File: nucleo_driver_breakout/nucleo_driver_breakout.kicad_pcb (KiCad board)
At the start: 4 copper layers, 211 x 123 mm, 118 parts, among them J1 Conn_02x18_Odd_Even, J10 Conn_01x06_Pin, J11 Conn_01x06_Pin, J12 Conn_01x04_Pin, J13 Conn_01x04_Pin, J14 Conn_01x04_Pin, J15 Conn_01x04_Pin, J16 Conn_01x02_Pin, J17 Conn_01x02_Pin, J18 Conn_01x02_Pin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

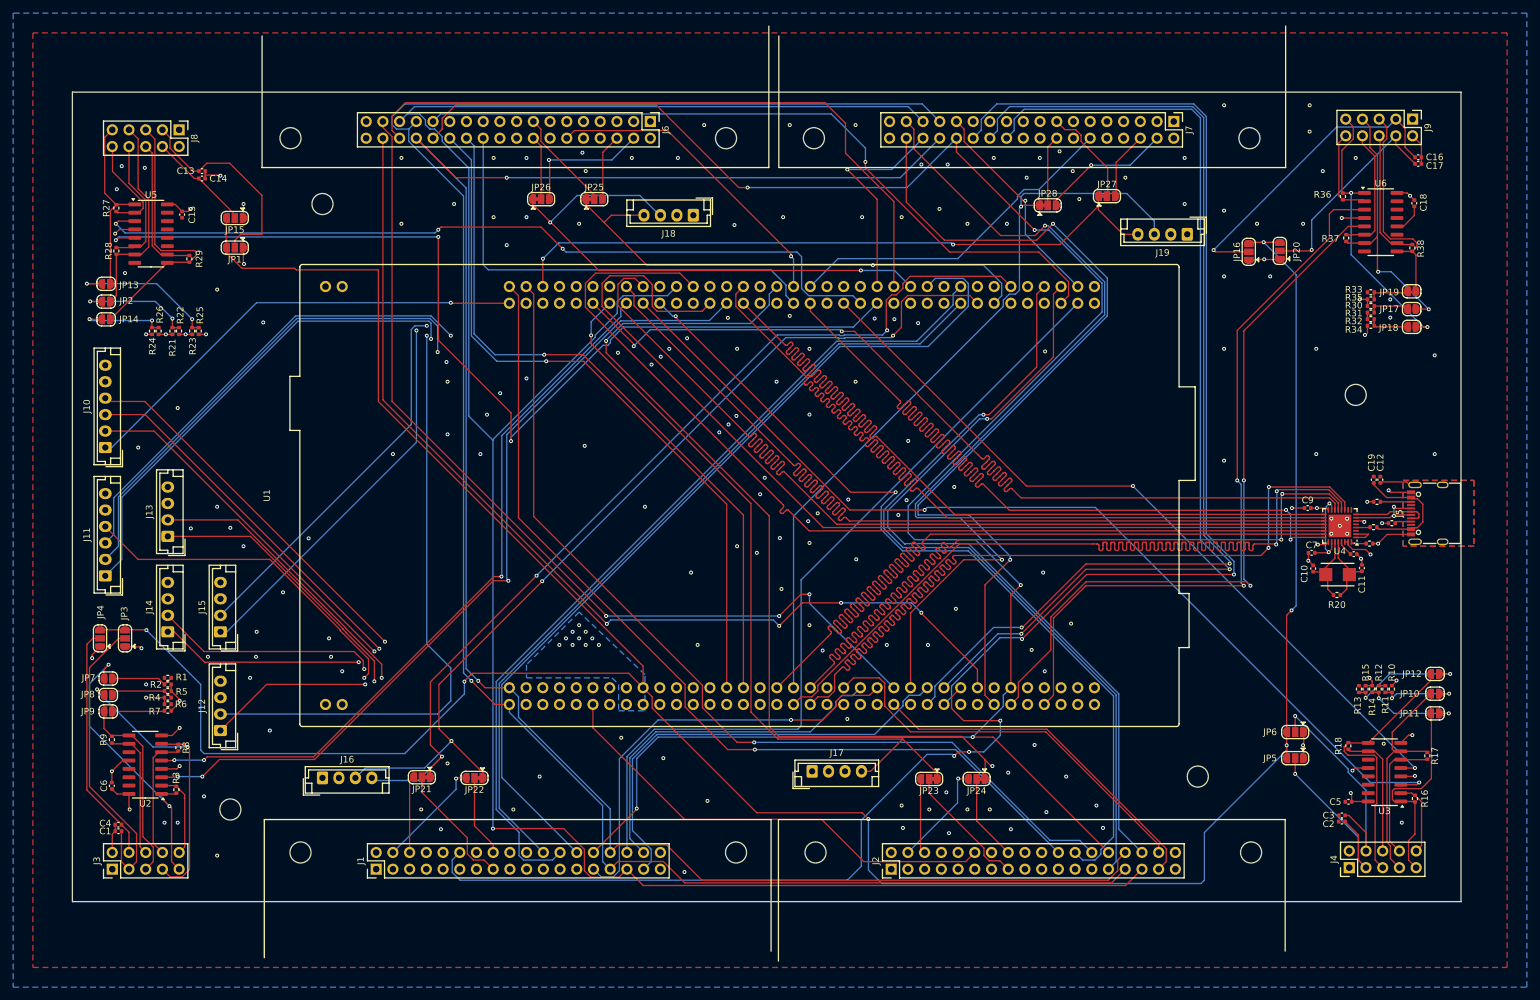
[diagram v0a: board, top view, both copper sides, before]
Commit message: changed termination resistors to 1206 and added gitignore
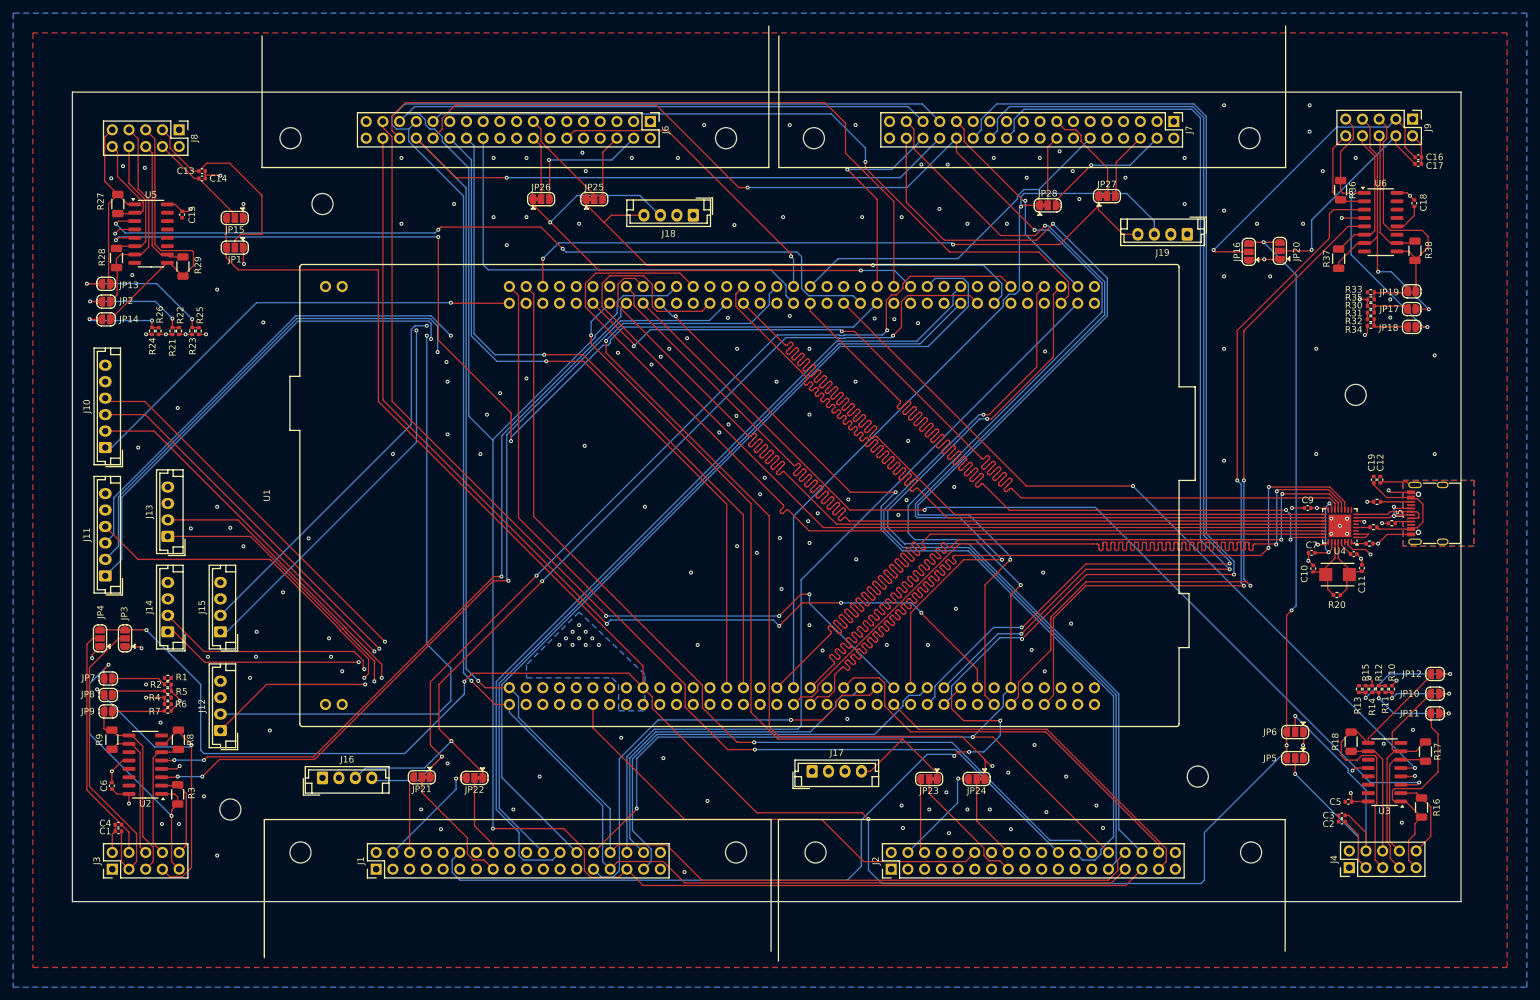
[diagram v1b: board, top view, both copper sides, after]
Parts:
- R16, R17, R18, R27, R28, R29, R3, R36, R37, R38, R8, R9: footprint Resistor_SMD:R_0402_1005Metric -> Resistor_SMD:R_1206_3216Metric
- moved R37 3.34 mm to (285.4, 86.3)
- moved R16 1.68 mm to (298.0, 169.7)
- moved R29 1.52 mm to (109.8, 87.5)
- moved R8 1.20 mm to (109.1, 159.4)
- moved R28 1.07 mm to (99.7, 86.2)
- moved R36 1.02 mm to (285.7, 75.9)
- moved R18 0.77 mm to (287.3, 159.7)
- moved R3 0.73 mm to (109.0, 167.7)
- moved R17 0.70 mm to (298.6, 161.2)
- moved R27 0.66 mm to (99.9, 78.0)
- moved R38 0.59 mm to (297.0, 85.1)
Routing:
- net GND: track 73.3 -> 67.8 mm
- net ENC2_I -: track 41.7 -> 45.3 mm
- net ENC1_B -: track 46.7 -> 50.1 mm
- net ENC4_B -: track 41.5 -> 44.6 mm
- net ENC4_I -: track 33.8 -> 36.9 mm
- net ENC4_B +: track 19.8 -> 21.9 mm
- net ENC3_I -: track 42.3 -> 44.1 mm
- net ENC2_A +: track 11.5 -> 13.0 mm
- net ENC1_A -: track 45.2 -> 46.4 mm
- net ENC4_A +: track 13.8 -> 14.7 mm
- net +3V3: track 84.0 -> 83.1 mm
- net ENC2_A -: track 32.4 -> 33.3 mm
- net ENC3_I +: track 21.8 -> 20.9 mm
- net ENC3_A -: track 27.8 -> 28.6 mm
- net ENC2_I +: track 19.8 -> 19.2 mm
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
